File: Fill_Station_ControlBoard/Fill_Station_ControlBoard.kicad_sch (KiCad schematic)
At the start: 40 parts, among them SW1 CK_KMS2xxG, SW2 BOOT, U1 STM32H747IITx, Y1 Crystal 25MHz, Y2 Crystal 32.768 kHz

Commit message: Modifs de l'organisation des pages
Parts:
- removed BT1: RTC_BAT, 0CSL_D1_V1:BatteryHolder_BHX1_1025, symbol 0CSL_D1_V1:Battery_Holder_1025
- removed C1, C14, C15, C16, C17, C18, C19, C2, C20, C3, C33, C34, C4, C5, C8: *, Capacitor_SMD:C_0603_1608Metric, symbol Device:C
- removed C23, C24, C25, C31: 2.2u, Capacitor_SMD:C_0603_1608Metric, symbol Device:C
- removed C26, C27: 6pF, Capacitor_SMD:C_0603_1608Metric, symbol Device:C
- removed C32: 100n, Capacitor_SMD:C_0603_1608Metric, symbol Device:C
- removed D2, D4, D5: LED, LED_SMD:LED_0603_1608Metric, symbol Device:LED
- removed R14, R39: 10k, Resistor_SMD:R_0603_1608Metric_Pad0.98x0.95mm_HandSolder, symbol Device:R_US
- removed R15, R16, R40: 0, Resistor_SMD:R_0603_1608Metric_Pad0.98x0.95mm_HandSolder, symbol Device:R_US
- removed R27: 100k, Resistor_SMD:R_0603_1608Metric_Pad0.98x0.95mm_HandSolder, symbol Device:R_US
- removed R53: 4.42k, Resistor_SMD:R_0805_2012Metric, symbol Device:R_US
- removed R54: 620, Resistor_SMD:R_0603_1608Metric_Pad0.98x0.95mm_HandSolder, symbol Device:R_US
- removed R55: 280, Resistor_SMD:R_0603_1608Metric_Pad0.98x0.95mm_HandSolder, symbol Device:R_US
- removed SW1: CK_KMS2xxG, Button_Switch_SMD:SW_SPST_CK_KMS2xxGP, symbol Switch:CK_KMS2xxG
- removed SW2: BOOT, symbol Switch:SW_Push_SPDT
- removed U1: STM32H747IITx, Package_QFP:LQFP-176_24x24mm_P0.5mm, symbol MCU_ST_STM32H7:STM32H747IITx
- removed Y1: Crystal 25MHz, Crystal:Crystal_SMD_3225-4Pin_3.2x2.5mm, symbol Device:Crystal
- removed Y2: Crystal 32.768 kHz, Crystal:Crystal_SMD_3225-4Pin_3.2x2.5mm, symbol Device:Crystal
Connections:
- no-connect marks 82 -> 0
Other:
- sheet Communication renamed Ethernet
- removed sheet Connecteur
- removed sheet Heaters
- added sheet Alimentation (Alimentation.kicad_sch)
- added sheet CAN FD (CANFD.kicad_sch)
- added sheet MCU (MCU.kicad_sch)
- added sheet USB (USB.kicad_sch)
- sheet Control ports: added GPIO1, GPIO2, GPIO3, GPIO4, GPIO5, GPIO6, Servo.Signal1, Servo.Signal2, Servo.Signal3; removed Servo.Signal1_1, Servo.Signal1_2, Servo.Signal1_ex, Servo.Signal2_1, Servo.Signal2_2, Servo.Signal2_ex
- sheet Ethernet ports: added none; removed CAN.FAULT, CAN.RXD, CAN.STBY, CAN.TXD, Eth.CLKIN
- note removed: "DEL d'alim"
- note removed: "Découplage"
- note removed: "Laisser flotante?"

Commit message: début layout
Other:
- sheet MCU ports: added GPIO1, GPIO2, GPIO3, GPIO4, GPIO5, GPIO6, Servo.Signal1, Servo.Signal2, Servo.Signal3; removed JTDO, NJTRST

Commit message: Ajout power
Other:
- sheet Alimentation ports: added LED1, LED2, LED3; removed none
- sheet MCU ports: added CAN.FAULT, LED1, LED2, LED3; removed CAN.STBY, Eth.RXER

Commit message: début layout
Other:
- sheet Control ports: added E-match1, E-match1_Cont, E-match1_Det, E-match2, E-match2_Cont, E-match2_Det, Heater1, Heater2, Heater3; removed none
- sheet Ethernet ports: added Clock25Mhz; removed Eth.RXER
- sheet MCU ports: added Clock25Mhz; removed none
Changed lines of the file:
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@@
+	(wire
+		(pts
+			(xy 254 162.56) (xy 304.8 162.56)
+		)
+		(stroke
+			(width 0)
+			(type default)
+		)
+	)
 	(wire
 		(pts
@@
 			)
 		)
-		(pin "Eth.RXER" output
-			(at 304.8 144.78 180)
-			(effects
-				(font
-					(size 1.27 1.27)
-				)
-				(justify left)
-			)
-		)
 		(pin "Eth.MDIO" bidirectional
 			(at 304.8 148.59 180)
@@
 		(pin "Eth.CRS_DV" output
 			(at 304.8 156.21 180)
+			(effects
+				(font
+					(size 1.27 1.27)
+				)
+				(justify left)
+			)
+		)
+		(pin "Clock25Mhz" input
+			(at 304.8 162.56 180)
 			(effects
 				(font
@@
 	)
 	(sheet
-		(at 304.8 50.8)
-		(size 38.1 38.1)
+		(at 304.8 25.4)
+		(size 38.1 63.5)
 		(exclude_from_sim no)
 		(in_bom yes)
@@
 		)
 		(property "Sheetname" "Control"
-			(at 304.8 50.0884 0)
+			(at 304.8 24.6884 0)
 			(effects
 				(font
@@
 		(pin "GPIO4" input
 			(at 304.8 80.01 180)
+			(effects
+				(font
+					(size 1.27 1.27)
+				)
+				(justify left)
+			)
+		)
+		(pin "E-match1_Cont" input
+			(at 304.8 33.02 180)
+			(effects
+				(font
+					(size 1.27 1.27)
+				)
+				(justify left)
+			)
+		)
+		(pin "E-match1_Det" output
+			(at 304.8 30.48 180)
+			(effects
+				(font
+					(size 1.27 1.27)
+				)
+				(justify left)
+			)
+		)
+		(pin "Heater2" input
+			(at 304.8 50.8 180)
+			(effects
+				(font
+					(size 1.27 1.27)
+				)
+				(justify left)
+			)
+		)
+		(pin "Heater1" input
+			(at 304.8 48.26 180)
+			(effects
+				(font
+					(size 1.27 1.27)
+				)
+				(justify left)
+			)
+		)
+		(pin "Heater3" input
+			(at 304.8 53.34 180)
+			(effects
+				(font
+					(size 1.27 1.27)
+				)
+				(justify left)
+			)
+		)
+		(pin "E-match1" input
+			(at 304.8 27.94 180)
+			(effects
+				(font
+					(size 1.27 1.27)
+				)
+				(justify left)
+			)
+		)
+		(pin "E-match2_Cont" input
+			(at 304.8 43.18 180)
+			(effects
+				(font
+					(size 1.27 1.27)
+				)
+				(justify left)
+			)
+		)
+		(pin "E-match2_Det" output
+			(at 304.8 40.64 180)
+			(effects
+				(font
+					(size 1.27 1.27)
+				)
+				(justify left)
+			)
+		)
+		(pin "E-match2" input
+			(at 304.8 38.1 180)
 			(effects
 				(font
@@
 	)
 	(sheet
-		(at 177.8 46.99)
-		(size 76.2 119.38)
+		(at 177.8 22.86)
+		(size 76.2 143.51)
 		(exclude_from_sim no)
 		(in_bom yes)
@@
 		)
 		(property "Sheetname" "MCU"
-			(at 177.8 46.2784 0)
+			(at 177.8 22.1484 0)
 			(effects
 				(font
@@
 			)
 		)
+		(pin "Clock25Mhz" output
+			(at 254 162.56 0)
+			(effects
+				(font
+					(size 1.27 1.27)
+				)
+				(justify right)
+			)
+		)

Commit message: PCB fait
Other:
- sheet CAN FD ports: added CAN.IN; removed CAN.FAULT
- sheet MCU ports: added E-Match1, E-Match1_Cont, E-Match1_Det, E-Match2, E-Match2_Cont, E-Match2_Det, Heater1, Heater2, Heater3, SD1.CLK, SD1.CMD, SD1.DAT0, SD1.DAT1, SD1.DAT2, SD1.DAT3, SD2.CLK, SD2.CMD, SD2.DAT0, SD2.DAT1, SD2.DAT2, SD2.DAT3; removed SD.CLK, SD.CMD, SD.DAT0, SD.DAT1, SD.DAT2, SD.DAT3
- sheet Storage ports: added SD1.CLK, SD1.CMD, SD1.DAT0, SD1.DAT1, SD1.DAT2, SD1.DAT3, SD2.CLK, SD2.CMD, SD2.DAT0, SD2.DAT1, SD2.DAT2, SD2.DAT3; removed SD.CLK, SD.CMD, SD.DAT0, SD.DAT1, SD.DAT2, SD.DAT3

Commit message: Travail Layout
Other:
- added sheet Monitor (Monitor.kicad_sch)
- sheet CAN FD ports: added none; removed CAN.IN
- sheet Ethernet ports: added Eth.RXD_N, Eth.RXD_P, Eth.TXD_N, Eth.TXD_P; removed Clock25Mhz, Eth.RXD0, Eth.RXD1, Eth.TXD0, Eth.TXD1
- sheet MCU ports: added Eth.RXD_N, Eth.RXD_P, Eth.TXD_N, Eth.TXD_P, SD2.DET; removed CAN.FAULT, Clock25Mhz, Eth.RXD0, Eth.RXD1, Eth.TXD0, Eth.TXD1
- sheet Storage ports: added SD2.DET; removed none

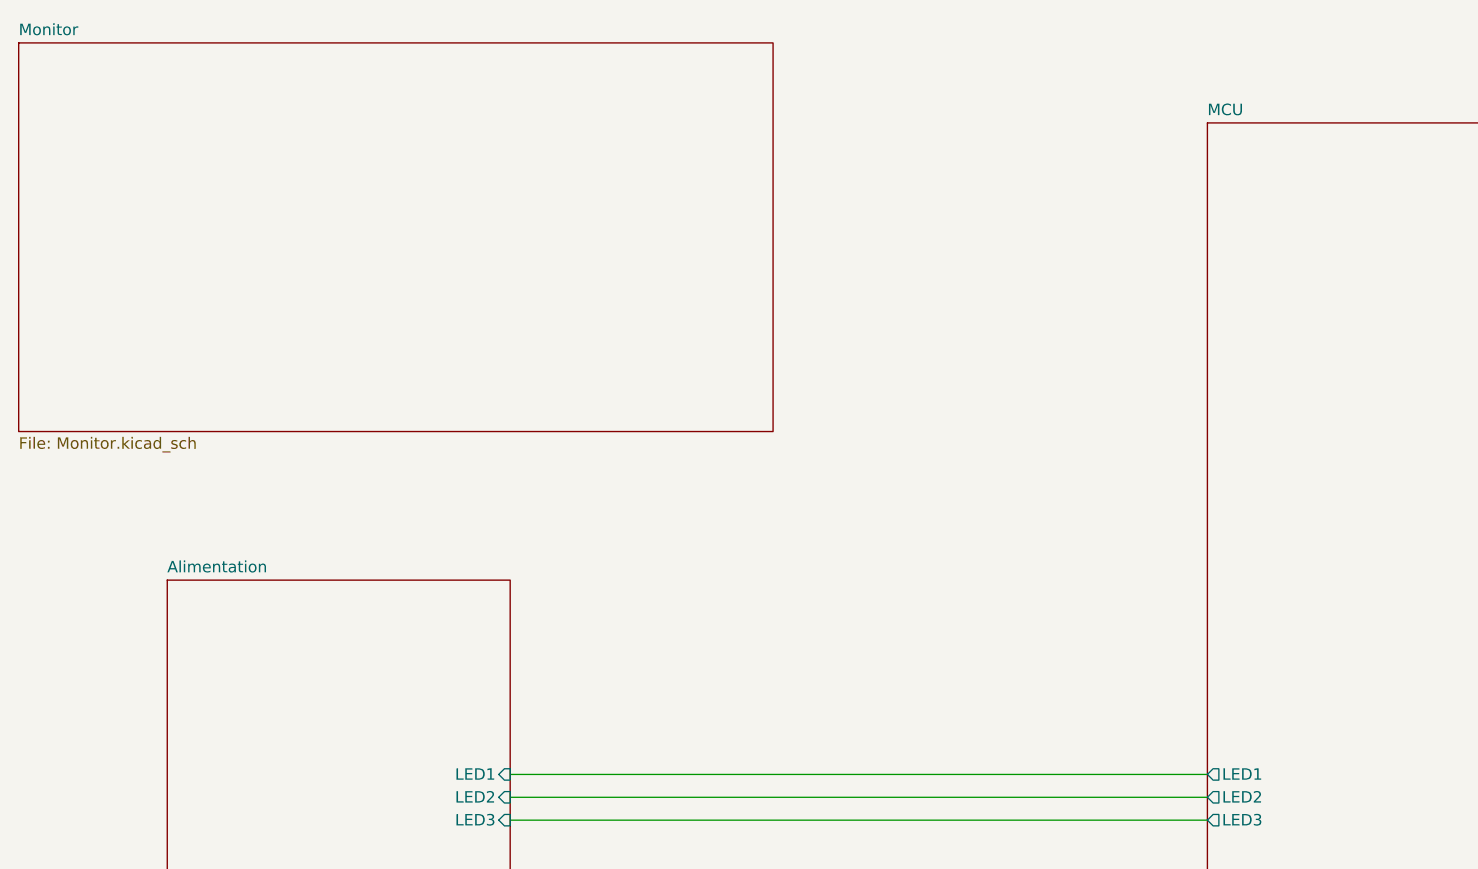
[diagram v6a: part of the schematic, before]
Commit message: PCB presque terminé
Modifs de l'alim
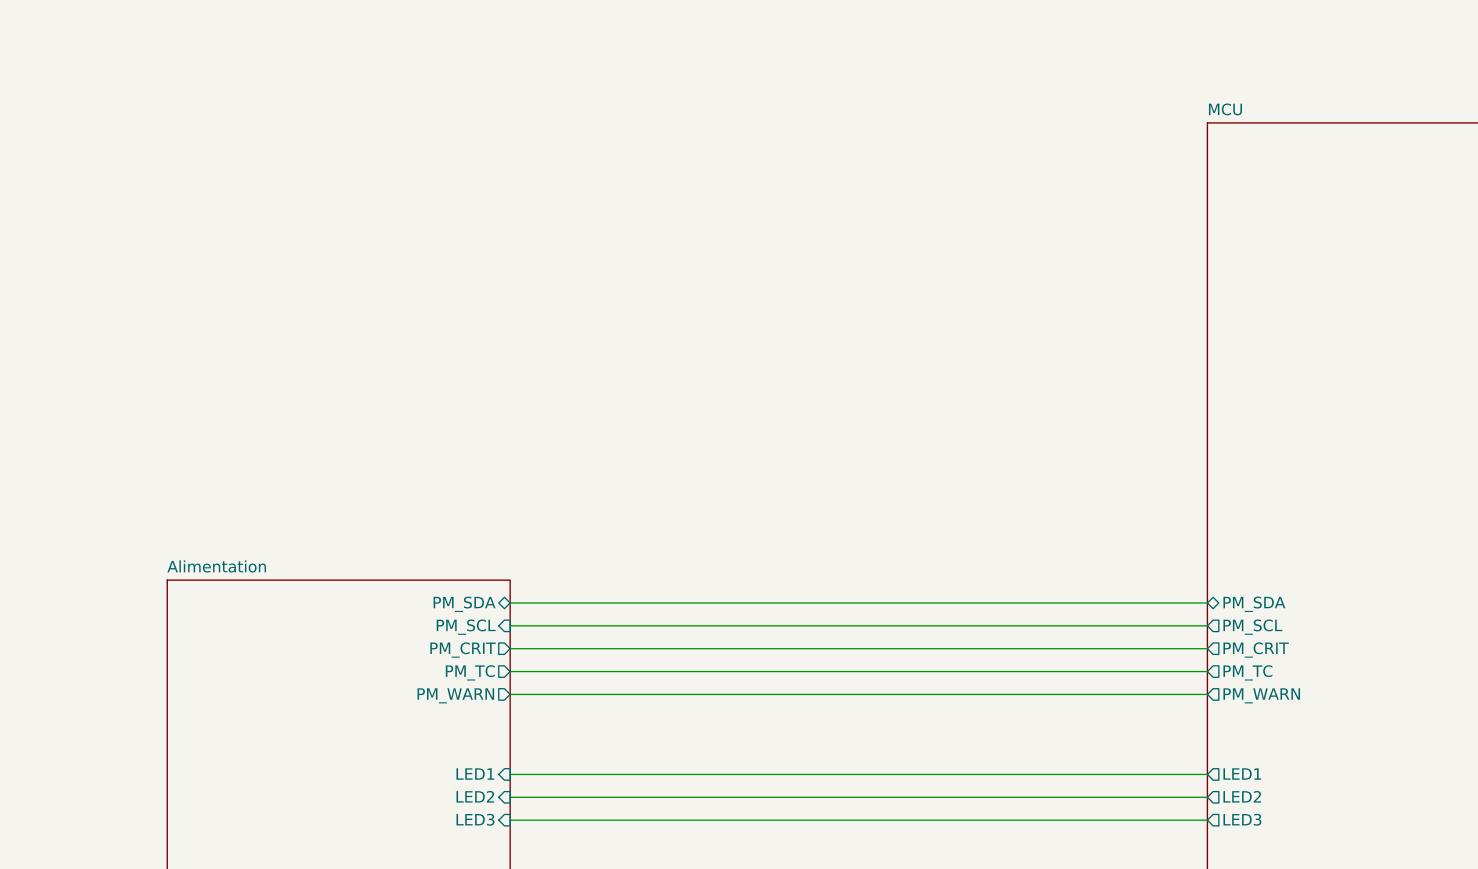
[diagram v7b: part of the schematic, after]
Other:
- removed sheet Monitor
- sheet Alimentation ports: added PM_CRIT, PM_SCL, PM_SDA, PM_TC, PM_WARN; removed none
- sheet MCU ports: added PM_CRIT, PM_SCL, PM_SDA, PM_TC, PM_WARN; removed none
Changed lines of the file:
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@@
+	(wire
+		(pts
+			(xy 176.53 99.06) (xy 99.06 99.06)
+		)
+		(stroke
+			(width 0)
+			(type default)
+		)
+	)
 	(wire
 		(pts
@@
 	(wire
 		(pts
+			(xy 99.06 106.68) (xy 176.53 106.68)
+		)
+		(stroke
+			(width 0)
+			(type default)
+		)
+	)
+	(wire
+		(pts
 			(xy 252.73 50.8) (xy 303.53 50.8)
 		)
@@
 	(wire
 		(pts
+			(xy 99.06 109.22) (xy 176.53 109.22)
+		)
+		(stroke
+			(width 0)
+			(type default)
+		)
+	)
+	(wire
+		(pts
 			(xy 252.73 173.99) (xy 303.53 173.99)
 		)
@@
 	(wire
 		(pts
+			(xy 99.06 104.14) (xy 176.53 104.14)
+		)
+		(stroke
+			(width 0)
+			(type default)
+		)
+	)
+	(wire
+		(pts
 			(xy 252.73 105.41) (xy 303.53 105.41)
 		)
@@
 		(pts
 			(xy 252.73 55.88) (xy 303.53 55.88)
+		)
+		(stroke
+			(width 0)
+			(type default)
+		)
+	)
+	(wire
+		(pts
+			(xy 99.06 101.6) (xy 176.53 101.6)
 		)
 		(stroke
@@
 	)
 	(sheet
-		(at 44.45 36.83)
-		(size 83.82 43.18)
-		(exclude_from_sim no)
-		(in_bom yes)
-		(on_board yes)
-		(dnp no)
-		(fields_autoplaced yes)
-		(stroke
-			(width 0.1524)
-			(type solid)
-		)
-		(fill
-			(color 0 0 0 0.0000)
-		)
-		(property "Sheetname" "Monitor"
-			(at 44.45 36.1184 0)
-			(effects
-				(font
-					(size 1.27 1.27)
-				)
-				(justify left bottom)
-			)
-		)
-		(property "Sheetfile" "Monitor.kicad_sch"
-			(at 44.45 80.5946 0)
-			(effects
-				(font
-					(size 1.27 1.27)
-				)
-				(justify left top)
-			)
-		)
-		(instances
-			(project "Fill_Station_ControlBoard"
-				(path "/eaacffe0-ee57-428e-a37e-5655e0922ccc"
-					(page "9")
-				)
-			)
-		)
-	)
-	(sheet
 		(at 60.96 96.52)
 		(size 38.1 38.1)
@@
 		(pin "LED3" input
 			(at 99.06 123.19 0)
+			(effects
+				(font
+					(size 1.27 1.27)
+				)
+				(justify right)
+			)
+		)
+		(pin "PM_SDA" bidirectional
+			(at 99.06 99.06 0)
+			(effects
+				(font
+					(size 1.27 1.27)
+				)
+				(justify right)
+			)
+		)
+		(pin "PM_SCL" input
+			(at 99.06 101.6 0)
+			(effects
+				(font
+					(size 1.27 1.27)
+				)
+				(justify right)
+			)
+		)
+		(pin "PM_CRIT" output
+			(at 99.06 104.14 0)
+			(effects
+				(font
+					(size 1.27 1.27)
+				)
+				(justify right)
+			)
+		)
+		(pin "PM_TC" output
+			(at 99.06 106.68 0)
+			(effects
+				(font
+					(size 1.27 1.27)
+				)
+				(justify right)
+			)
+		)
+		(pin "PM_WARN" output
+			(at 99.06 109.22 0)
 			(effects
 				(font
@@
 			)
 		)
+		(pin "PM_SDA" bidirectional
+			(at 176.53 99.06 180)
+			(effects
+				(font
+					(size 1.27 1.27)
+				)
+				(justify left)
+			)
+		)
+		(pin "PM_SCL" output
+			(at 176.53 101.6 180)
+			(effects
+				(font
+					(size 1.27 1.27)
+				)
+				(justify left)
+			)
+		)
+		(pin "PM_WARN" output
+			(at 176.53 109.22 180)
+			(effects
+				(font
+					(size 1.27 1.27)
+				)
+				(justify left)
+			)
+		)
+		(pin "PM_CRIT" output
+			(at 176.53 104.14 180)
+			(effects
+				(font
+					(size 1.27 1.27)
+				)
+				(justify left)
+			)
+		)
+		(pin "PM_TC" output
+			(at 176.53 106.68 180)
+			(effects
+				(font
+					(size 1.27 1.27)
+				)
+				(justify left)
+			)
+		)

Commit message: finalisé le pcb
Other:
- sheet Control ports: added BUZZ; removed GPIO6
- sheet MCU ports: added none; removed GPIO6
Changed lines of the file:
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@@
-	(wire
-		(pts
-			(xy 252.73 107.95) (xy 303.53 107.95)
-		)
-		(stroke
-			(width 0)
-			(type default)
-		)
-	)
 	(wire
 		(pts
@@
 			)
 		)
-		(pin "GPIO6" input
-			(at 303.53 107.95 180)
-			(effects
-				(font
-					(size 1.27 1.27)
-				)
-				(justify left)
-			)
-		)
 		(pin "GPIO3" input
 			(at 303.53 100.33 180)
@@
 		(pin "E-match2" input
 			(at 303.53 60.96 180)
+			(effects
+				(font
+					(size 1.27 1.27)
+				)
+				(justify left)
+			)
+		)
+		(pin "BUZZ" input
+			(at 303.53 109.22 180)
 			(effects
 				(font
@@
 			(effects
 				(font
-					(size 1.27 1.27)
-				)
-				(justify right)
-			)
-		)
-		(pin "GPIO6" input
-			(at 252.73 107.95 0)
-			(effects
-				(font
